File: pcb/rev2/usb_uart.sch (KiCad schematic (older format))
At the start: 13 parts, among them CN9 TYCO_1734035-1, IC6 FT230XS-T

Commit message: pcb wip
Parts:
- C76, C80, C81: footprint CAPC1608X87N -> Capacitors SMD:CAPC1608X87N
- C77, C79, C82: footprint CAPC1608X90N -> Capacitors SMD:CAPC1608X90N
- D5: footprint SOD3715X145N -> ICs And Semiconductors SMD:SOD3715X145N
- D6: footprint DIOM5226X262N -> ICs And Semiconductors SMD:DIOM5226X262N
- IC6: footprint SOP63P600X175-16N -> ICs And Semiconductors SMD:SOP63P600X175-16N
- L7: footprint INDC2012X105N -> Inductors SMD:INDC2012X105N
- R54, R55: footprint RESC1608X55N -> Resistors SMD:RESC1608X55N
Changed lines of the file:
@@
 F 0 "D6" V 4746 3010 50  0000 R CNN
 F 1 "SMAJ5.0A" V 4655 3010 50  0000 R CNN
-F 2 "DIOM5226X262N" H 4550 1960 60  0001 L CNN
+F 2 "ICs And Semiconductors SMD:DIOM5226X262N" H 4550 1960 60  0001 L CNN
 F 3 "\\cern.ch\\dfs\\Applications\\Altium\\Datasheets\\SMAJ5.0A.pdf" H 4550 2680 60  0001 L CNN
 F 4 "SMAJ5.0A" H 4550 2590 60  0001 L CNN "Part Number"
@@
 F 0 "D5" V 4296 3190 50  0000 L CNN
 F 1 "MBR0530PbF" V 4205 3190 50  0000 L CNN
-F 2 "SOD3715X145N" H 4100 1960 60  0001 L CNN
+F 2 "ICs And Semiconductors SMD:SOD3715X145N" H 4100 1960 60  0001 L CNN
 F 3 "\\cern.ch\\dfs\\Applications\\Altium\\Datasheets\\MBR0530PBF.pdf" H 4100 2680 60  0001 L CNN
 F 4 "MBR0530PbF" H 4100 2590 60  0001 L CNN "Part Number"
@@
 F 0 "C79" V 5104 2910 50  0000 L CNN
 F 1 "CC0603_100NF_100V_10%_X7R" H 5000 2540 60  0001 L CNN
-F 2 "CAPC1608X90N" H 5000 1730 60  0001 L CNN
+F 2 "Capacitors SMD:CAPC1608X90N" H 5000 1730 60  0001 L CNN
 F 3 "\\cern.ch\\dfs\\Applications\\Altium\\Datasheets\\CC0603_MURATA_GRM188R72A104KA35D.pdf" H 5000 2360 60  0001 L CNN
 F 4 "100nF" V 5195 2910 50  0000 L CNN "~"
@@
 F 0 "L7" H 4550 3867 50  0000 C CNN
 F 1 "IND0805_MURATA_BLM21PG221SN1D" H 4400 3460 60  0001 L CNN
-F 2 "INDC2012X105N" H 4400 2650 60  0001 L CNN
+F 2 "Inductors SMD:INDC2012X105N" H 4400 2650 60  0001 L CNN
 F 3 "\\cern.ch\\dfs\\Applications\\Altium\\Datasheets\\IND0805_MURATA_BLM21P.pdf" H 4400 3280 60  0001 L CNN
 F 4 "220R@100MHz" H 4550 3776 50  0000 C CNN "~"
@@
 F 0 "C81" V 4504 4060 50  0000 L CNN
 F 1 "CC0603_33PF_50V_5%_NP0" H 4400 3690 60  0001 L CNN
-F 2 "CAPC1608X87N" H 4400 2880 60  0001 L CNN
+F 2 "Capacitors SMD:CAPC1608X87N" H 4400 2880 60  0001 L CNN
 F 3 "\\cern.ch\\dfs\\Applications\\Altium\\Datasheets\\CC0603_NP0_PHYCOMP.pdf" H 4400 3510 60  0001 L CNN
 F 4 "33pF" V 4595 4060 50  0000 L CNN "~"
@@
 F 0 "C80" V 4904 4060 50  0000 L CNN
 F 1 "CC0603_33PF_50V_5%_NP0" H 4800 3690 60  0001 L CNN
-F 2 "CAPC1608X87N" H 4800 2880 60  0001 L CNN
+F 2 "Capacitors SMD:CAPC1608X87N" H 4800 2880 60  0001 L CNN
 F 3 "\\cern.ch\\dfs\\Applications\\Altium\\Datasheets\\CC0603_NP0_PHYCOMP.pdf" H 4800 3510 60  0001 L CNN
 F 4 "33pF" V 4995 4060 50  0000 L CNN "~"
@@
 F 0 "R54" H 5375 3850 50  0000 C CNN
 F 1 "R0603_33R_1%_0.1W_100PPM" H 5250 3540 60  0001 L CNN
-F 2 "RESC1608X55N" H 5250 2730 60  0001 L CNN
+F 2 "Resistors SMD:RESC1608X55N" H 5250 2730 60  0001 L CNN
 F 3 "\\cern.ch\\dfs\\Applications\\Altium\\Datasheets\\R0603_NIC_NRC.pdf" H 5250 3360 60  0001 L CNN
 F 4 "33" H 5550 3850 50  0000 C CNN "~"
@@
 F 0 "R55" H 5300 3750 50  0000 C CNN
 F 1 "R0603_33R_1%_0.1W_100PPM" H 5250 3640 60  0001 L CNN
-F 2 "RESC1608X55N" H 5250 2830 60  0001 L CNN
+F 2 "Resistors SMD:RESC1608X55N" H 5250 2830 60  0001 L CNN
 F 3 "\\cern.ch\\dfs\\Applications\\Altium\\Datasheets\\R0603_NIC_NRC.pdf" H 5250 3460 60  0001 L CNN
 F 4 "33" H 5450 3750 50  0000 C CNN "~"
@@
 F 0 "IC6" H 6600 3615 50  0000 C CNN
 F 1 "FT230XS-T" H 6600 3524 50  0000 C CNN
-F 2 "SOP63P600X175-16N" H 6100 1060 60  0001 L CNN
+F 2 "ICs And Semiconductors SMD:SOP63P600X175-16N" H 6100 1060 60  0001 L CNN
 F 3 "\\cern.ch\\dfs\\Applications\\Altium\\Datasheets\\FT230XS-T.pdf" H 6100 1780 60  0001 L CNN
 F 4 "FT230XS-T" H 6100 1690 60  0001 L CNN "Part Number"
@@
 F 0 "C77" V 5904 3160 50  0000 L CNN
 F 1 "CC0603_100NF_100V_10%_X7R" H 5800 2790 60  0001 L CNN
-F 2 "CAPC1608X90N" H 5800 1980 60  0001 L CNN
+F 2 "Capacitors SMD:CAPC1608X90N" H 5800 1980 60  0001 L CNN
 F 3 "\\cern.ch\\dfs\\Applications\\Altium\\Datasheets\\CC0603_MURATA_GRM188R72A104KA35D.pdf" H 5800 2610 60  0001 L CNN
 F 4 "100nF" V 5995 3160 50  0000 L CNN "~"
@@
 F 0 "C76" V 5554 3160 50  0000 L CNN
 F 1 "CC0603_1UF_50V_10%_X5R" H 5450 2790 60  0001 L CNN
-F 2 "CAPC1608X87N" H 5450 1980 60  0001 L CNN
+F 2 "Capacitors SMD:CAPC1608X87N" H 5450 1980 60  0001 L CNN
 F 3 "\\cern.ch\\dfs\\Applications\\Altium\\Datasheets\\CC0603_X5R_TDK_C.pdf" H 5450 2610 60  0001 L CNN
 F 4 "1uF" V 5645 3160 50  0000 L CNN "~"
@@
 F 0 "C82" V 5554 4441 50  0000 R CNN
 F 1 "CC0603_100NF_100V_10%_X7R" H 5450 4290 60  0001 L CNN
-F 2 "CAPC1608X90N" H 5450 3480 60  0001 L CNN
+F 2 "Capacitors SMD:CAPC1608X90N" H 5450 3480 60  0001 L CNN
 F 3 "\\cern.ch\\dfs\\Applications\\Altium\\Datasheets\\CC0603_MURATA_GRM188R72A104KA35D.pdf" H 5450 4110 60  0001 L CNN
 F 4 "100nF" V 5645 4441 50  0000 R CNN "~"

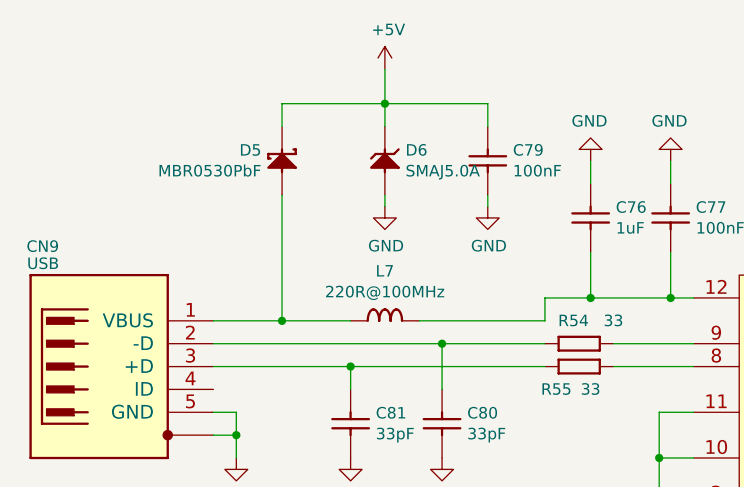
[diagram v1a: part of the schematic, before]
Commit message: Completed port to KiCad, passes DRC+LVS. NOT MANUFACTURED.
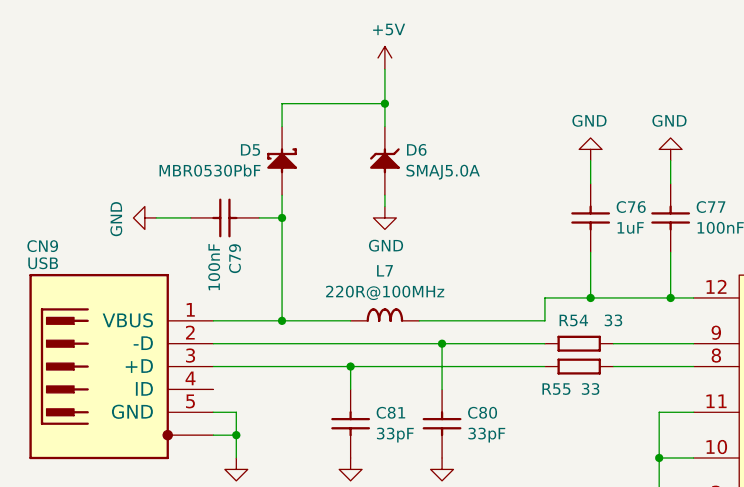
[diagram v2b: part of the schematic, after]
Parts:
- CN9: footprint TYCO_1734035-1 -> TYCO SMD:TYCO_1734035-1; Fieldname (none) -> Value
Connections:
- net +5V: no longer C79.1
- net at CN9.1 (VBUS), D5.2 (A), L7.1: now also C79.1
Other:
- moved on the sheet: C79

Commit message: axi4/zynq version: wip
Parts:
- C76: symbol CC0603_1UF_50V_10%_X5R -> dsi_shield-rescue:CC0603_1UF_50V_10%_X5R-
- C77, C79, C82: symbol CC0603_100NF_100V_10%_X7R -> dsi_shield-rescue:CC0603_100NF_100V_10%_X7R-
- C80, C81: symbol CC0603_33PF_50V_5%_NP0 -> dsi_shield-rescue:CC0603_33PF_50V_5%_NP0-
- CN9: symbol TYCO_1734035-1 -> dsi_shield-rescue:TYCO_1734035-1-
- D5: symbol MBR0530PbF -> dsi_shield-rescue:MBR0530PbF-
- D6: symbol SMAJ5.0A -> dsi_shield-rescue:SMAJ5.0A-
- IC6: symbol FT230XS-T -> dsi_shield-rescue:FT230XS-T-
- L7: symbol IND0805_MURATA_BLM21PG221SN1D -> dsi_shield-rescue:IND0805_MURATA_BLM21PG221SN1D-
- R54, R55: symbol R0603_33R_1%_0.1W_100PPM -> dsi_shield-rescue:R0603_33R_1%_0.1W_100PPM-
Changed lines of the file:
@@
-EESchema Schematic File Version 2
-LIBS:Capacitors Networks THD
-LIBS:Capacitors Networks SMD
-LIBS:Capacitors THD
-LIBS:Capacitors SMD
-LIBS:Miscellaneous
-LIBS:HARWIN
-LIBS:LEMO
-LIBS:WEIDMULLER
-LIBS:FCI
-LIBS:MOLEX
-LIBS:TYCO
-LIBS:ERNI
-LIBS:MENTOR
-LIBS:SAMTEC
-LIBS:STELVIO-KONTEK COMATEL
-LIBS:AMPHENOL
-LIBS:HARTING
-LIBS:3M
-LIBS:Pads
-LIBS:Switches
-LIBS:Relays
-LIBS:Heat-Sinks
-LIBS:Fasteners & Fixings
-LIBS:Batteries
-LIBS:Fuses
-LIBS:Metal Screening Box
-LIBS:Sockets
-LIBS:Regulators
-LIBS:Transistors
-LIBS:Power Supplies
-LIBS:Analog & Interface
-LIBS:Sensors
-LIBS:Logic
-LIBS:Optocouplers
-LIBS:Standard Logic
-LIBS:DC-DC Converters
-LIBS:Operational Amplifiers
-LIBS:Crystals & Oscillators
-LIBS:Diodes
-LIBS:LEDs & Displays
-LIBS:PCB Modules
-LIBS:Bonding
-LIBS:Resistors THD
-LIBS:Potentiometers SMD
-LIBS:Thermistors And Varistors
-LIBS:Potentiometers THD
-LIBS:Resistor Networks THD
-LIBS:Resistors SMD
-LIBS:Resistor Networks SMD
-LIBS:Transformers
-LIBS:Inductors SMD
-LIBS:Inductors THD
-LIBS:Cores
-LIBS:power
-LIBS:conn
-LIBS:dsi_shield
+EESchema Schematic File Version 4
 LIBS:dsi_shield-cache
 EELAYER 26 0
@@
 $EndDescr
 $Comp
-L TYCO_1734035-1 CN9
+L dsi_shield-rescue:TYCO_1734035-1- CN9
 U 1 1 599785FD
 P 3600 3450
@@
 $EndComp
 $Comp
-L SMAJ5.0A D6
+L dsi_shield-rescue:SMAJ5.0A- D6
 U 1 1 5997A427
 P 4550 3100
@@
 $EndComp
 $Comp
-L MBR0530PbF D5
+L dsi_shield-rescue:MBR0530PbF- D5
 U 1 1 5997AB4D
 P 4100 3100
@@
 Connection ~ 3900 4150
 $Comp
-L GND #PWR099
+L dsi_shield-rescue:GND- #PWR099
 U 1 1 5997AFF5
 P 3900 4250
@@
 $EndComp
 $Comp
-L CC0603_100NF_100V_10%_X7R C79
+L dsi_shield-rescue:CC0603_100NF_100V_10%_X7R- C79
 U 1 1 5997CE02
 P 4000 3200
@@
 	4100 3100 4100 3650
 $Comp
-L IND0805_MURATA_BLM21PG221SN1D L7
+L dsi_shield-rescue:IND0805_MURATA_BLM21PG221SN1D- L7
 U 1 1 59980767
 P 4400 3650
@@
 $EndComp
 $Comp
-L CC0603_33PF_50V_5%_NP0 C81
+L dsi_shield-rescue:CC0603_33PF_50V_5%_NP0- C81
 U 1 1 599828F0
 P 4400 3950
@@
 $EndComp
 $Comp
-L CC0603_33PF_50V_5%_NP0 C80
+L dsi_shield-rescue:CC0603_33PF_50V_5%_NP0- C80
 U 1 1 59982A38
 P 4800 3950
@@
 Connection ~ 4800 3750
 $Comp
-L R0603_33R_1%_0.1W_100PPM R54
+L dsi_shield-rescue:R0603_33R_1%_0.1W_100PPM- R54
 U 1 1 599835D1
 P 5250 3750
@@
 $EndComp
 $Comp
-L R0603_33R_1%_0.1W_100PPM R55
+L dsi_shield-rescue:R0603_33R_1%_0.1W_100PPM- R55
 U 1 1 5998373E
 P 5250 3850
@@
 $EndComp
 $Comp
-L GND #PWR0100
+L dsi_shield-rescue:GND- #PWR0100
 U 1 1 599837C0
 P 4550 3150
@@
 	4550 3150 4550 3100
 $Comp
-L GND #PWR0101
+L dsi_shield-rescue:GND- #PWR0101
 U 1 1 599837FA
 P 3550 3200
@@
 $EndComp
 $Comp
-L +5V #PWR0102
+L dsi_shield-rescue:+5V- #PWR0102
 U 1 1 599839AA
 P 4550 2550
@@
 $EndComp
 $Comp
-L FT230XS-T IC6
+L dsi_shield-rescue:FT230XS-T- IC6
 U 1 1 59985415
 P 6100 3450
@@
 	5250 3550 5900 3550
 $Comp
-L CC0603_100NF_100V_10%_X7R C77
+L dsi_shield-rescue:CC0603_100NF_100V_10%_X7R- C77
 U 1 1 59985C6F
 P 5800 3050
@@
 $EndComp
 $Comp
-L CC0603_1UF_50V_10%_X5R C76
+L dsi_shield-rescue:CC0603_1UF_50V_10%_X5R- C76
 U 1 1 59986995
 P 5450 3050
@@
 Connection ~ 5800 3550
 $Comp
-L GND #PWR0103
+L dsi_shield-rescue:GND- #PWR0103
 U 1 1 59986BD4
 P 5450 2950
@@
 	5450 3050 5450 2950
 $Comp
-L GND #PWR0104
+L dsi_shield-rescue:GND- #PWR0104
 U 1 1 59986C3A
 P 5800 2950
@@
 Connection ~ 5750 4250
 $Comp
-L CC0603_100NF_100V_10%_X7R C82
+L dsi_shield-rescue:CC0603_100NF_100V_10%_X7R- C82
 U 1 1 59988276
 P 5450 4550
@@
 Connection ~ 5450 4900
 $Comp
-L GND #PWR0105
+L dsi_shield-rescue:GND- #PWR0105
 U 1 1 599883E4
 P 5450 5000
@@
 $EndComp
 $Comp
-L GND #PWR0106
+L dsi_shield-rescue:GND- #PWR0106
 U 1 1 59989979
 P 7400 5000
@@
 ~CPU_RST
 $Comp
-L GND #PWR0107
+L dsi_shield-rescue:GND- #PWR0107
 U 1 1 5998B74E
 P 7400 3850
@@
 	7300 4350 7600 4350
 $Comp
-L GND #PWR0108
+L dsi_shield-rescue:GND- #PWR0108
 U 1 1 5998E794
 P 4400 4250
@@
 $EndComp
 $Comp
-L GND #PWR0109
+L dsi_shield-rescue:GND- #PWR0109
 U 1 1 5998E7EA
 P 4800 4250
